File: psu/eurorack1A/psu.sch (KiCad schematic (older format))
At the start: 37 parts, among them J1 Conn_01x02_Male, J10 Conn_02x08_Odd_Even, J11 Conn_02x08_Odd_Even, J12 Conn_02x08_Odd_Even, J13 Conn_02x08_Odd_Even, J2 Conn_01x02_Male, J3 Conn_01x02_Male, J4 Conn_02x08_Odd_Even, J5 Conn_02x08_Odd_Even, J6 Conn_02x08_Odd_Even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

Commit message: Preparations for next revision
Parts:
- removed SW1: SW_MEC_5G_LED, Connector_PinHeader_2.54mm:PinHeader_1x04_P2.54mm_Vertical, symbol Switch:SW_MEC_5G_LED
- added R4, R5: R, Resistor_THT:R_Axial_DIN0207_L6.3mm_D2.5mm_P10.16mm_Horizontal, symbol Device:R
- added SW2: Conn_02x03_Odd_Even, Connector_PinHeader_2.54mm:PinHeader_2x03_P2.54mm_Vertical, symbol Connector_Generic:Conn_02x03_Odd_Even
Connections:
- net +12V: now also R4.1
- net -12V: now also R5.1
- net GND: now also SW2.3 (Pin_3)
- net VIN: now also SW2.2 (Pin_2)
- net at J1.1 (Pin_1), J2.1 (Pin_1), J3.1 (Pin_1): now also SW2.1 (Pin_1)
- net at R1.2: now also SW2.4 (Pin_4)
- new net: R4.2, SW2.6 (Pin_6)
- new net: R5.2, SW2.5 (Pin_5)
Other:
- note added: "1/2 Switch\n3 GND\n4 +5V\n5 -12V\n6 +12V"
- note added: "Option 1"
- note added: "Option 2"
- moved on the sheet: C1, C2, C3, C4, C5, C6, C7, C8, D1, D2, D3, H1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

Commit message: dropped option 1
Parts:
- removed C7, C8: 22u/50V, Capacitor_THT:CP_Radial_D6.3mm_P2.50mm, symbol Device:CP
- removed D2, D3: 1N5406RLG, Diode_THT:D_DO-41_SOD81_P10.16mm_Horizontal, symbol Diode:1N4001
- removed R2, R3: 0R, Resistor_THT:R_Axial_DIN0207_L6.3mm_D2.5mm_P10.16mm_Horizontal, symbol Device:R
- removed U5: VR20S12, Package_TO_SOT_THT:TO-220-3_Vertical, symbol Regulator_Linear:LM7815_TO220
- D1: footprint Diode_THT:D_DO-41_SOD81_P10.16mm_Horizontal -> Diode_THT:D_DO-201AD_P15.24mm_Horizontal
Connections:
- net GND: now also D1.2 (A)
- net VIN: now also D1.1 (K), U1.1 (VIN); no longer D1.2 (A)
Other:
- note removed: "Option 1"
- note removed: "Option 2"
- moved on the sheet: D1, U1
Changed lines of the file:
@@
 EESchema Schematic File Version 4
+LIBS:psu-cache
 EELAYER 30 0
 EELAYER END
@@
 L PSU:PYBE30 U1
 U 1 1 5F5B1323
-P 4600 2450
-F 0 "U1" H 4650 2500 50  0000 C CNN
-F 1 "PYBE30-Q24-D15" H 4950 1900 50  0000 C CNN
-F 2 "psu:PYBE30" H 4600 2450 50  0001 C CNN
-F 3 "" H 4600 2450 50  0001 C CNN
-	1    4600 2450
+P 5100 1450
+F 0 "U1" H 5150 1500 50  0000 C CNN
+F 1 "PYBE30-Q24-D15" H 5450 900 50  0000 C CNN
+F 2 "psu:PYBE30" H 5100 1450 50  0001 C CNN
+F 3 "" H 5100 1450 50  0001 C CNN
+	1    5100 1450
 	1    0    0    -1
 $EndComp
@@
 L power:GND #PWR0102
 U 1 1 5F5B2AFF
-P 4400 3000
-F 0 "#PWR0102" H 4400 2750 50  0001 C CNN
-F 1 "GND" H 4405 2827 50  0000 C CNN
-F 2 "" H 4400 3000 50  0001 C CNN
-F 3 "" H 4400 3000 50  0001 C CNN
-	1    4400 3000
-	1    0    0    -1
-$EndComp
-Wire Wire Line
-	4500 2850 4400 2850
-Wire Wire Line
-	4400 2850 4400 3000
+P 4900 2000
+F 0 "#PWR0102" H 4900 1750 50  0001 C CNN
+F 1 "GND" H 4905 1827 50  0000 C CNN
+F 2 "" H 4900 2000 50  0001 C CNN
+F 3 "" H 4900 2000 50  0001 C CNN
+	1    4900 2000
+	1    0    0    -1
+$EndComp
+Wire Wire Line
+	5000 1850 4900 1850
+Wire Wire Line
+	4900 1850 4900 1950
 Wire Wire Line
 	7850 2400 8000 2400
@@
 L Diode:1N4001 D1
 U 1 1 5F5C0503
-P 4250 2550
-F 0 "D1" H 4250 2333 50  0000 C CNN
-F 1 "1N5406RLG" H 4250 2424 50  0000 C CNN
-F 2 "Diode_THT:D_DO-41_SOD81_P10.16mm_Horizontal" H 4250 2375 50  0001 C CNN
-F 3 "http://www.vishay.com/docs/88503/1n4001.pdf" H 4250 2550 50  0001 C CNN
-	1    4250 2550
-	-1   0    0    1
+P 4750 1750
+F 0 "D1" H 4750 1533 50  0000 C CNN
+F 1 "1N5406RLG" H 4900 1600 50  0000 C CNN
+F 2 "Diode_THT:D_DO-201AD_P15.24mm_Horizontal" H 4750 1575 50  0001 C CNN
+F 3 "http://www.vishay.com/docs/88503/1n4001.pdf" H 4750 1750 50  0001 C CNN
+	1    4750 1750
+	0    1    1    0
 $EndComp
 Connection ~ 9050 1400
@@
 $EndComp
 Connection ~ 1950 1650
-Text GLabel 3950 2550 0    50   Input ~ 0
+Text GLabel 4450 1550 0    50   Input ~ 0
 VIN
-Wire Wire Line
-	4400 2550 4500 2550
 Text GLabel 3350 1550 2    50   Input ~ 0
 VIN
@@
 Wire Wire Line
 	7850 1400 8000 1400
-Text GLabel 5550 2550 2    50   Input ~ 0
+Text GLabel 6050 1550 2    50   Input ~ 0
 +15V
 Wire Wire Line
-	5400 2550 5550 2550
-Wire Wire Line
-	5400 2700 5550 2700
-Wire Wire Line
-	5400 2850 5550 2850
-Text GLabel 5550 2850 2    50   Input ~ 0
+	5900 1550 6050 1550
+Wire Wire Line
+	5900 1700 6050 1700
+Wire Wire Line
+	5900 1850 6050 1850
+Text GLabel 6050 1850 2    50   Input ~ 0
 -15V
-Text GLabel 5550 2700 2    50   Input ~ 0
-0V
-$Comp
-L Regulator_Linear:LM7815_TO220 U5
-U 1 1 5F88E4C6
-P 5200 1400
-F 0 "U5" H 5200 1642 50  0000 C CNN
-F 1 "VR20S12" H 5200 1551 50  0000 C CNN
-F 2 "Package_TO_SOT_THT:TO-220-3_Vertical" H 5200 1625 50  0001 C CIN
-F 3 "http://www.fairchildsemi.com/ds/LM/LM7805.pdf" H 5200 1350 50  0001 C CNN
-	1    5200 1400
-	1    0    0    -1
-$EndComp
-$Comp
-L Device:CP C7
-U 1 1 5F8C77B7
-P 4650 1650
-F 0 "C7" H 4768 1696 50  0000 L CNN
-F 1 "22u/50V" H 4768 1605 50  0000 L CNN
-F 2 "Capacitor_THT:CP_Radial_D6.3mm_P2.50mm" H 4688 1500 50  0001 C CNN
-F 3 "~" H 4650 1650 50  0001 C CNN
-	1    4650 1650
-	1    0    0    -1
-$EndComp
-$Comp
-L Device:CP C8
-U 1 1 5F8C7F03
-P 5650 1650
-F 0 "C8" H 5768 1696 50  0000 L CNN
-F 1 "22u/50V" H 5768 1605 50  0000 L CNN
-F 2 "Capacitor_THT:CP_Radial_D6.3mm_P2.50mm" H 5688 1500 50  0001 C CNN
-F 3 "~" H 5650 1650 50  0001 C CNN
-	1    5650 1650
-	1    0    0    -1
-$EndComp
-Wire Wire Line
-	4650 1500 4650 1400
-Wire Wire Line
-	4650 1400 4900 1400
-Wire Wire Line
-	5500 1400 5650 1400
-Wire Wire Line
-	5650 1400 5650 1500
-Wire Wire Line
-	5200 1700 5200 1900
-Wire Wire Line
-	5200 1900 4650 1900
-Wire Wire Line
-	4650 1900 4650 1800
-Wire Wire Line
-	5650 1800 5650 1900
-Wire Wire Line
-	5650 1900 5200 1900
-Connection ~ 5200 1900
-Text GLabel 3950 1400 0    50   Input ~ 0
-VIN
-Connection ~ 5650 1400
-$Comp
-L Device:R R3
-U 1 1 5F9A222F
-P 5950 1900
-F 0 "R3" V 6050 1900 50  0000 C CNN
-F 1 "0R" V 5950 1900 50  0000 C CNN
-F 2 "Resistor_THT:R_Axial_DIN0207_L6.3mm_D2.5mm_P10.16mm_Horizontal" V 5880 1900 50  0001 C CNN
-F 3 "~" H 5950 1900 50  0001 C CNN
-	1    5950 1900
-	0    -1   -1   0
-$EndComp
-Wire Wire Line
-	5650 1900 5800 1900
-Connection ~ 5650 1900
-Text GLabel 6750 1400 2    50   Input ~ 0
-+15V
-Wire Wire Line
-	6600 1400 6750 1400
-$Comp
-L Device:R R2
-U 1 1 5F9F2240
-P 4400 1400
-F 0 "R2" V 4500 1400 50  0000 C CNN
-F 1 "0R" V 4400 1400 50  0000 C CNN
-F 2 "Resistor_THT:R_Axial_DIN0207_L6.3mm_D2.5mm_P10.16mm_Horizontal" V 4330 1400 50  0001 C CNN
-F 3 "~" H 4400 1400 50  0001 C CNN
-	1    4400 1400
-	0    -1   -1   0
-$EndComp
-Wire Wire Line
-	4550 1400 4650 1400
-Connection ~ 4650 1400
-Wire Wire Line
-	3950 1400 4250 1400
+Text GLabel 6050 1700 2    50   Input ~ 0
+0V
 Wire Wire Line
 	8600 1900 9050 1900
 Wire Wire Line
-	3950 2550 4100 2550
-$Comp
-L Diode:1N4001 D2
-U 1 1 5FB340FB
-P 6450 1400
-F 0 "D2" H 6450 1183 50  0000 C CNN
-F 1 "1N5406RLG" H 6450 1274 50  0000 C CNN
-F 2 "Diode_THT:D_DO-41_SOD81_P10.16mm_Horizontal" H 6450 1225 50  0001 C CNN
-F 3 "http://www.vishay.com/docs/88503/1n4001.pdf" H 6450 1400 50  0001 C CNN
-	1    6450 1400
-	-1   0    0    1
-$EndComp
-Wire Wire Line
 	8000 2000 8000 1900
 Wire Wire Line
@@
 Wire Wire Line
 	9050 2000 9050 1900
-Text GLabel 6750 1750 2    50   Input ~ 0
--15V
-Wire Wire Line
-	6600 1750 6750 1750
-$Comp
-L Diode:1N4001 D3
-U 1 1 5FBD9420
-P 6450 1750
-F 0 "D3" H 6450 1967 50  0000 C CNN
-F 1 "1N5406RLG" H 6450 1876 50  0000 C CNN
-F 2 "Diode_THT:D_DO-41_SOD81_P10.16mm_Horizontal" H 6450 1575 50  0001 C CNN
-F 3 "http://www.vishay.com/docs/88503/1n4001.pdf" H 6450 1750 50  0001 C CNN
-	1    6450 1750
-	1    0    0    -1
-$EndComp
-Wire Wire Line
-	5650 1400 6200 1400
-Wire Wire Line
-	6300 1750 6200 1750
-Wire Wire Line
-	6200 1750 6200 1400
-Connection ~ 6200 1400
-Wire Wire Line
-	6200 1400 6300 1400
-$Comp
-L power:GND #PWR0103
-U 1 1 5FC2DC23
-P 5200 2000
-F 0 "#PWR0103" H 5200 1750 50  0001 C CNN
-F 1 "GND" H 5205 1827 50  0000 C CNN
-F 2 "" H 5200 2000 50  0001 C CNN
-F 3 "" H 5200 2000 50  0001 C CNN
-	1    5200 2000
-	1    0    0    -1
-$EndComp
-Wire Wire Line
-	5200 2000 5200 1900
-Wire Wire Line
-	6750 1900 6100 1900
-Text GLabel 6750 1900 2    50   Input ~ 0
-0V
 Connection ~ 8000 1400
 Wire Wire Line
@@
 Wire Wire Line
 	3150 1650 3350 1650
-Wire Notes Line
-	3650 2250 7200 2250
-Wire Notes Line
-	7200 1050 3650 1050
-Wire Notes Line
-	3650 3450 7200 3450
-Wire Notes Line
-	7200 1050 7200 3450
-Wire Notes Line
-	3650 1050 3650 3450
-Text Notes 3700 2200 0    50   ~ 0
-Option 1
-Text Notes 3700 3400 0    50   ~ 0
-Option 2
 $Comp
 L Device:R R4
@@
 Text Notes 2300 2450 0    50   ~ 0
 1/2 Switch\n3 GND\n4 +5V\n5 -12V\n6 +12V
+Wire Wire Line
+	4450 1550 4750 1550
+Wire Wire Line
+	4750 1600 4750 1550
+Connection ~ 4750 1550
+Wire Wire Line
+	4750 1550 5000 1550
+Wire Wire Line
+	4750 1900 4750 1950
+Wire Wire Line
+	4750 1950 4900 1950
+Connection ~ 4900 1950
+Wire Wire Line
+	4900 1950 4900 2000
 $EndSCHEMATC

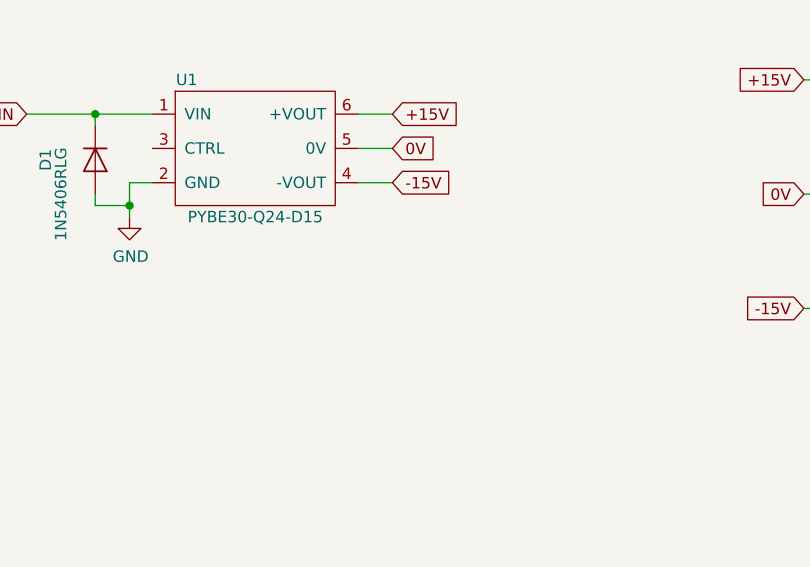
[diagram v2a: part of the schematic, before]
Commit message: added DKMW30
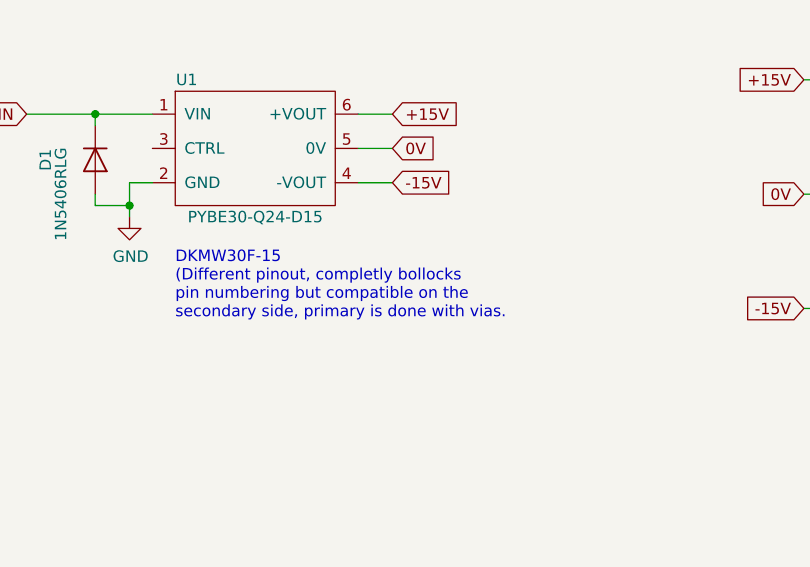
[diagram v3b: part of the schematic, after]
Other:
- note added: "DKMW30F-15\n(Different pinout, completly bollocks \npin numbering but compatible on the \nsecondary side, primary is done with vias."
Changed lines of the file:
@@
 Sheet 1 1
 Title "1A Eurorack PSU"
-Date "2020-09-13"
-Rev "00"
+Date "2020-10-05"
+Rev "01"
 Comp "Wiggis Modular"
 Comment1 ""
@@
 Wire Wire Line
 	4900 1950 4900 2000
+Text Notes 5100 2450 0    50   ~ 0
+DKMW30F-15\n(Different pinout, completly bollocks \npin numbering but compatible on the \nsecondary side, primary is done with vias.
 $EndSCHEMATC
